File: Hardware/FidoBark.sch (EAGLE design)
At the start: 30 parts, among them T1 BPX81

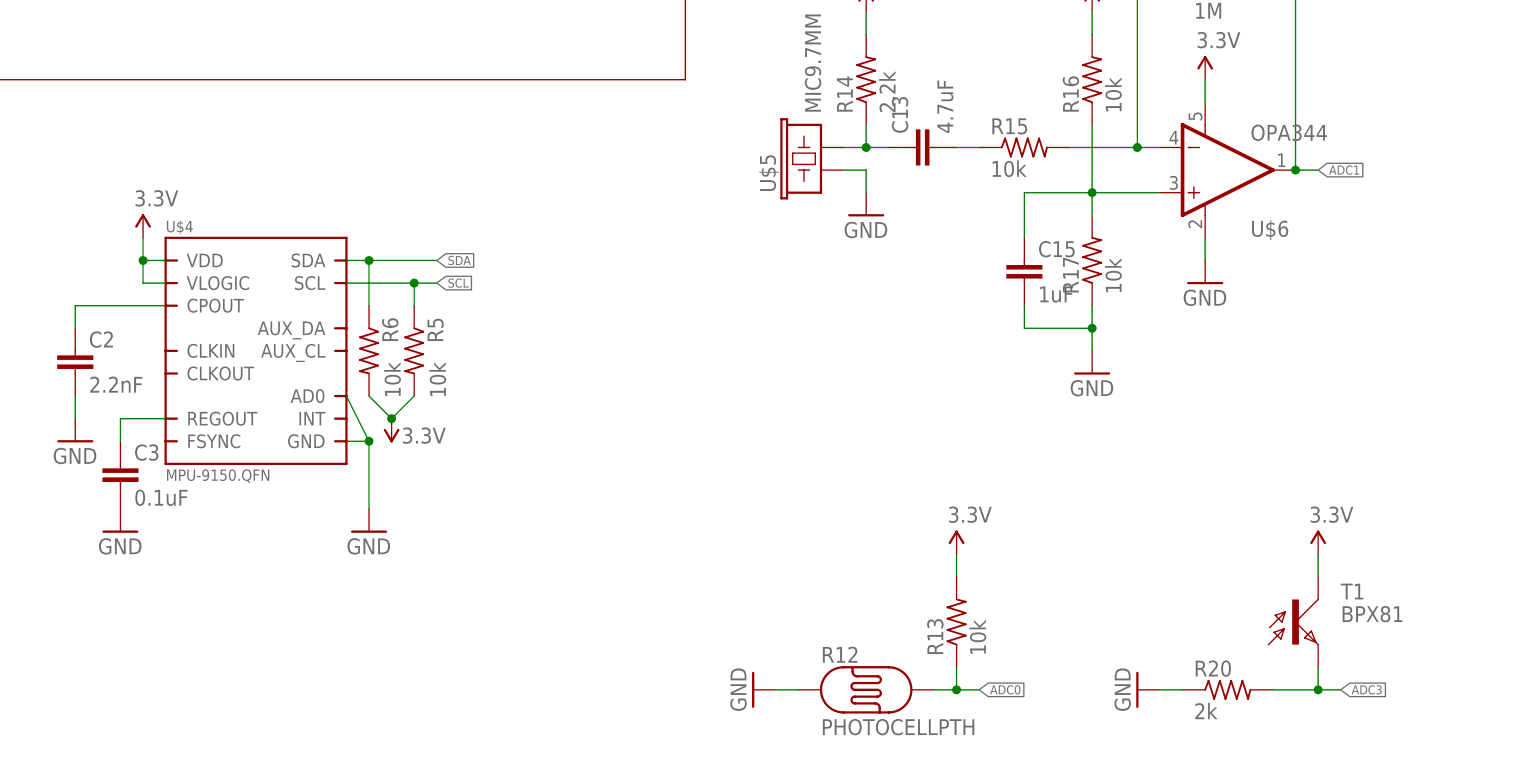
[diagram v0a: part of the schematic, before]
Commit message: battery level sense
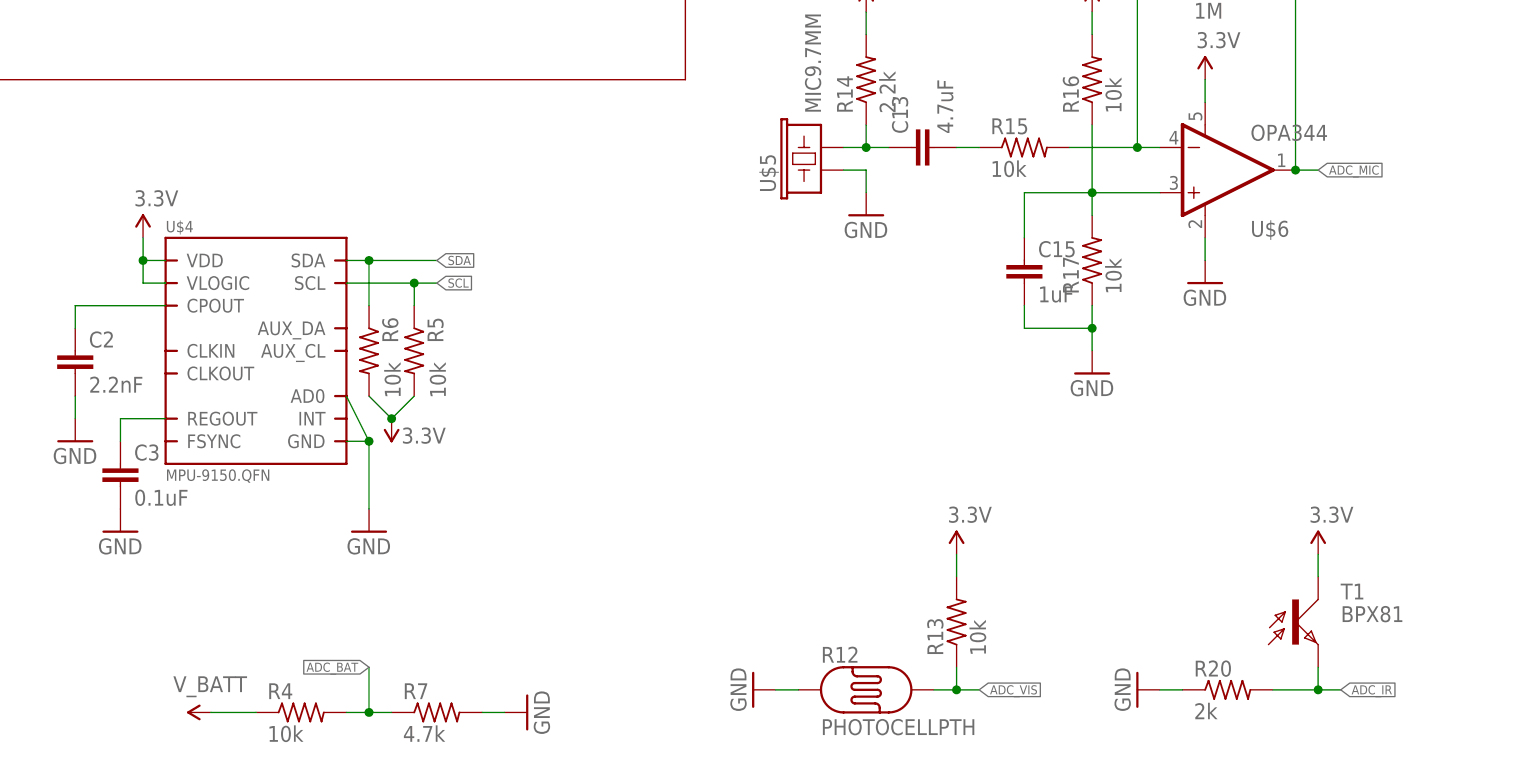
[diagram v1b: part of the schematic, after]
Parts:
- added R4: 10k, rcl:R-US_R0603
- added R7: 4.7k, rcl:R-US_R0603
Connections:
- net ADC0 renamed ADC_VIS
- net ADC1 renamed ADC_MIC
- net ADC3 renamed ADC_IR
- new net ADC_BAT: R4.2, R7.1
- net GND: now also R7.2
- net V_BATT: now also R4.1
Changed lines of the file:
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@@
 <part name="SUPPLY25" library="SparkFun-Aesthetics" deviceset="3.3V" device=""/>
 <part name="R20" library="adafruit" deviceset="R-US_" device="R0603" value="2k"/>
+<part name="R4" library="rcl" deviceset="R-US_" device="R0603" value="10k"/>
+<part name="R7" library="rcl" deviceset="R-US_" device="R0603" value="4.7k"/>
+<part name="SUPPLY7" library="SparkFun-Aesthetics" deviceset="V_BATT" device=""/>
+<part name="GND11" library="SparkFun-Aesthetics" deviceset="GND" device=""/>
 </parts>
 <sheets>
@@
 <instance part="SUPPLY25" gate="G$1" x="162.56" y="68.58"/>
 <instance part="R20" gate="G$1" x="152.4" y="53.34"/>
+<instance part="R4" gate="G$1" x="48.26" y="50.8"/>
+<instance part="R7" gate="G$1" x="63.5" y="50.8"/>
+<instance part="SUPPLY7" gate="G$1" x="38.1" y="50.8" smashed="yes" rot="R90">
+<attribute name="VALUE" x="42.164" y="54.864" size="1.778" layer="96" rot="R180"/>
+</instance>
+<instance part="GND11" gate="1" x="73.66" y="50.8" rot="R90"/>
 </instances>
 <busses>
@@
 <pinref part="R20" gate="G$1" pin="1"/>
 </segment>
+<segment>
+<pinref part="R7" gate="G$1" pin="2"/>
+<pinref part="GND11" gate="1" pin="GND"/>
+<wire x1="68.58" y1="50.8" x2="71.12" y2="50.8" width="0.1524" layer="91"/>
+</segment>
 </net>
 <net name="MOSI" class="0">
@@
 <junction x="63.5" y="205.74"/>
 </segment>
+<segment>
+<pinref part="SUPPLY7" gate="G$1" pin="V_BATT"/>
+<pinref part="R4" gate="G$1" pin="1"/>
+<wire x1="38.1" y1="50.8" x2="43.18" y2="50.8" width="0.1524" layer="91"/>
+</segment>
 </net>
 <net name="N$2" class="0">
@@
 </segment>
 </net>
-<net name="ADC0" class="0">
+<net name="ADC_VIS" class="0">
 <segment>
 <pinref part="R12" gate="G$1" pin="P$2"/>
@@
 </segment>
 </net>
-<net name="ADC1" class="0">
+<net name="ADC_MIC" class="0">
 <segment>
 <pinref part="U$6" gate="G$1" pin="OUT"/>
@@
 </segment>
 </net>
-<net name="ADC3" class="0">
+<net name="ADC_IR" class="0">
 <segment>
 <wire x1="157.48" y1="53.34" x2="162.56" y2="53.34" width="0.1524" layer="91"/>
@@
 </segment>
 </net>
+<net name="ADC_BAT" class="0">
+<segment>
+<pinref part="R4" gate="G$1" pin="2"/>
+<pinref part="R7" gate="G$1" pin="1"/>
+<wire x1="53.34" y1="50.8" x2="55.88" y2="50.8" width="0.1524" layer="91"/>
+<wire x1="55.88" y1="50.8" x2="58.42" y2="50.8" width="0.1524" layer="91"/>
+<wire x1="55.88" y1="50.8" x2="55.88" y2="55.88" width="0.1524" layer="91"/>
+<junction x="55.88" y="50.8"/>
+<label x="55.88" y="55.88" size="1.016" layer="95" rot="R180" xref="yes"/>
+</segment>
+</net>

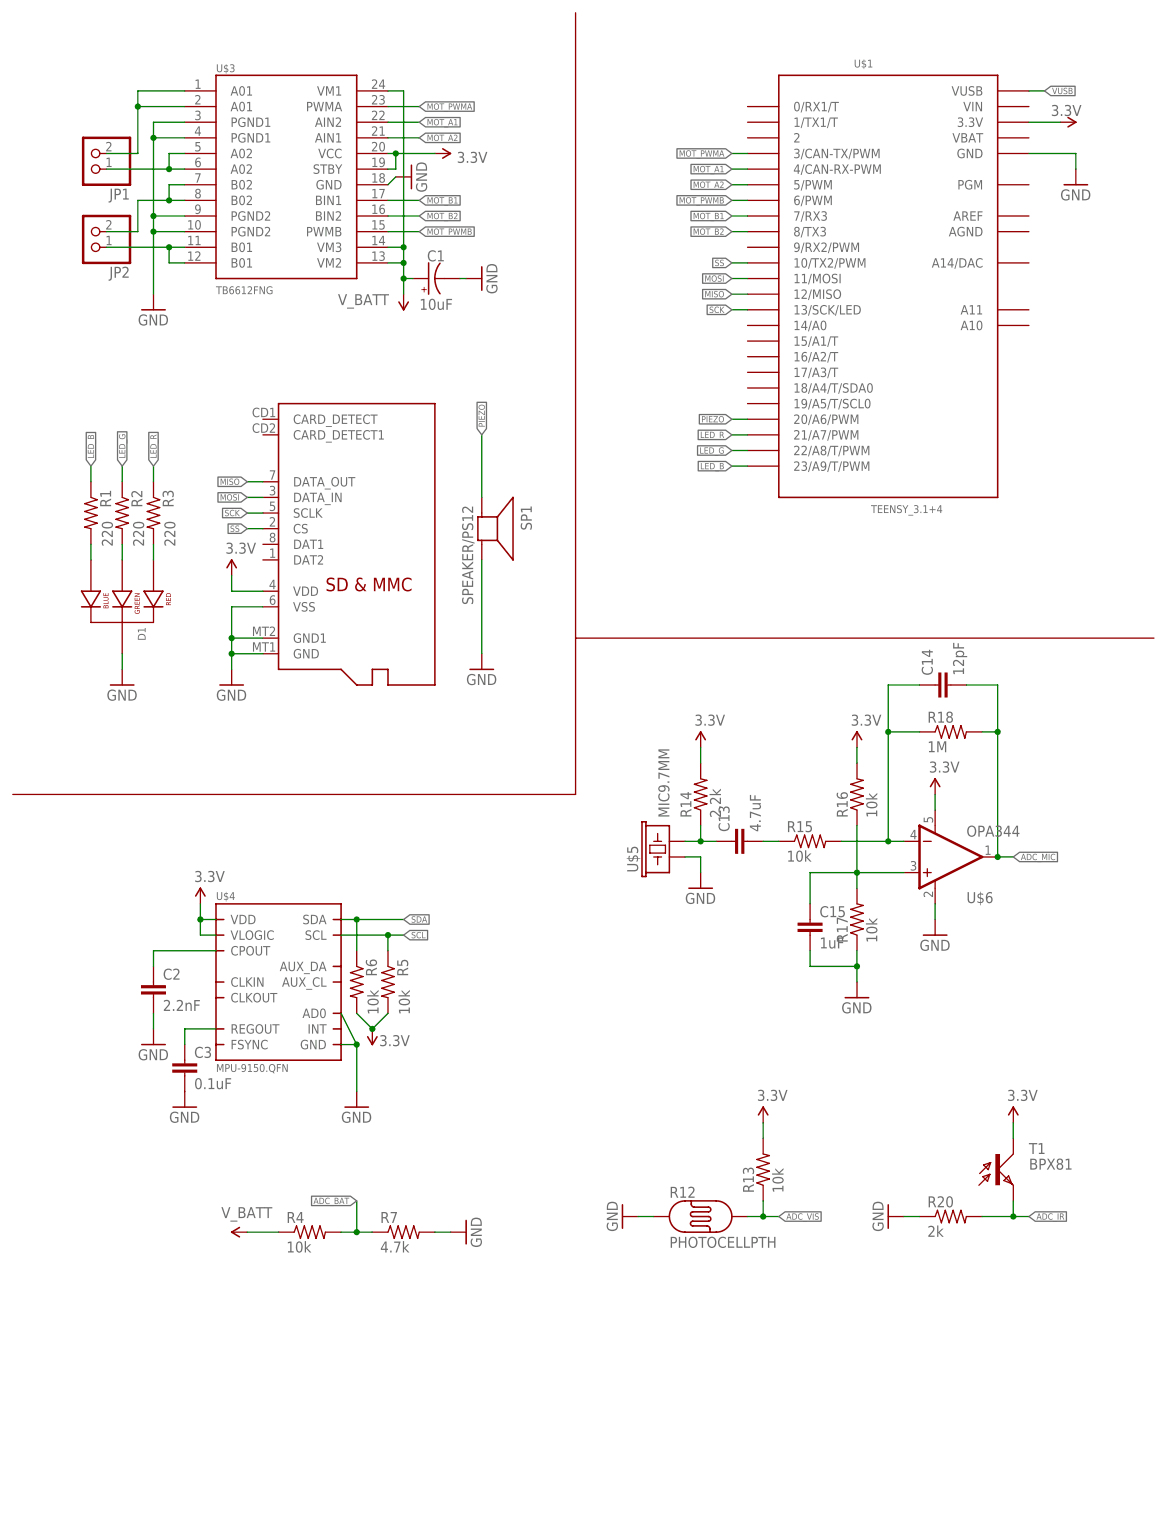
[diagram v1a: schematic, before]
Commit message: added Bluetooth 4.0 Low Energy
should be relatively simple now to interface over an IOS/Android app to
check battery life, download neural nets, etc
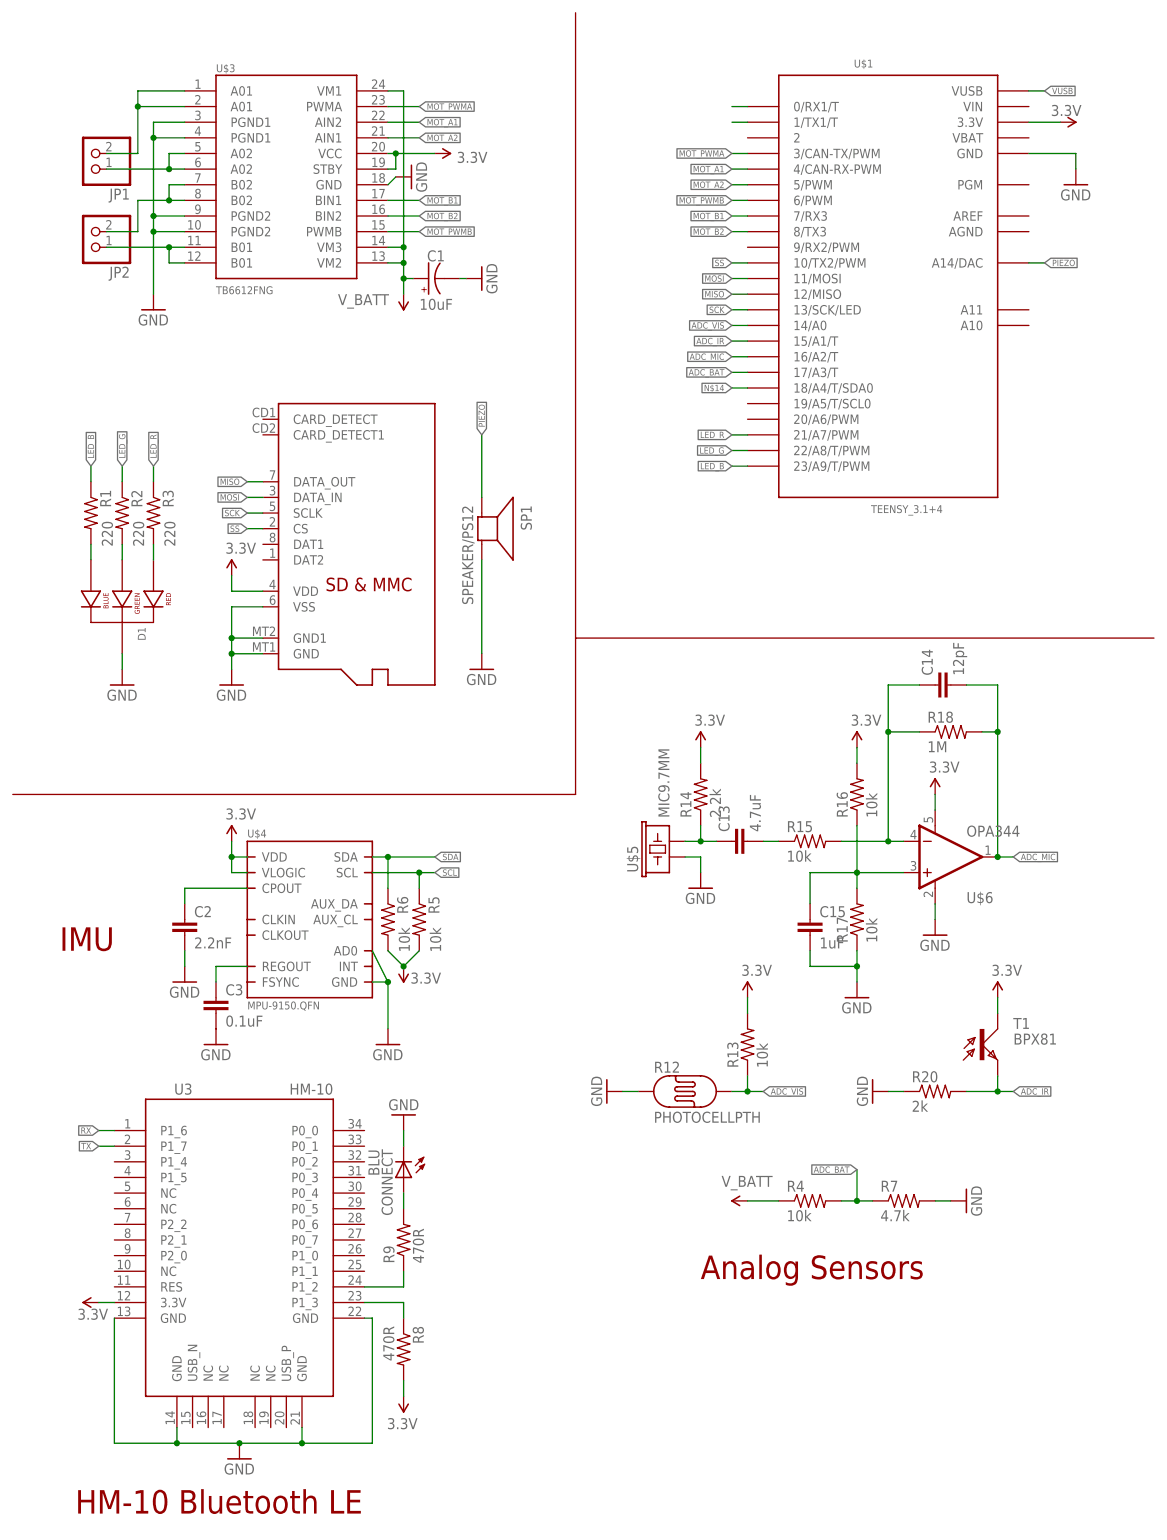
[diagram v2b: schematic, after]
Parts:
- added CONNECT: BLU, adafruit:LEDCHIPLED_0805
- added R8, R9: 470R, SparkFun-Resistors:0.3OHM-1/8W-1%(0805)
- added U3: HM-10, HM-10_BLE:HM-10
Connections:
- new net N$10: R9.1, U3.P1_2
- new net N$11: R8.1, U3.P1_3
- new net N$12: U$1.0/RX1/T
- new net N$13: U$1.1/TX1/T
- new net N$14: U$1.18/A4/T/SDA0
- new net N$16: CONNECT.A, R9.2
- new net RX: U3.P1_6
- new net TX: U3.P1_7
- net 3.3V: now also R8.2, U3.3.3V
- net ADC_BAT: now also U$1.17/A3/T
- net ADC_IR: now also U$1.15/A1/T
- net ADC_MIC: now also U$1.16/A2/T
- net ADC_VIS: now also U$1.14/A0
- net GND: now also CONNECT.C, U3.GND@1, U3.GND@2, U3.GND@3, U3.GND@4
- net PIEZO: now also U$1.A14/DAC; no longer U$1.20/A6/PWM
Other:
- note added: "Analog Sensors"
- note added: "HM-10 Bluetooth LE"
- note added: "IMU"
- moved on the sheet: C2, C3, R12, R13, R20, R4, R5, R6, R7, T1, U$4

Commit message: cosmetics and routing prep
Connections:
- removed net N$12: U$1.0/RX1/T
- removed net N$13: U$1.1/TX1/T
- removed net N$14: U$1.18/A4/T/SDA0
- net RX: now also U$1.0/RX1/T
- net TX: now also U$1.1/TX1/T
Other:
- note added: "1.0"
- note added: "Dual Motor Driver"
- note added: "Fido Prototype PCB"
- note added: "Joshua Gruenstein and Michael Truell"
- note added: "MicroSD Card"
- note added: "RGB LED"
- note added: "Teensy 3.1"
- moved on the sheet: C1, JP1, JP2, U$3

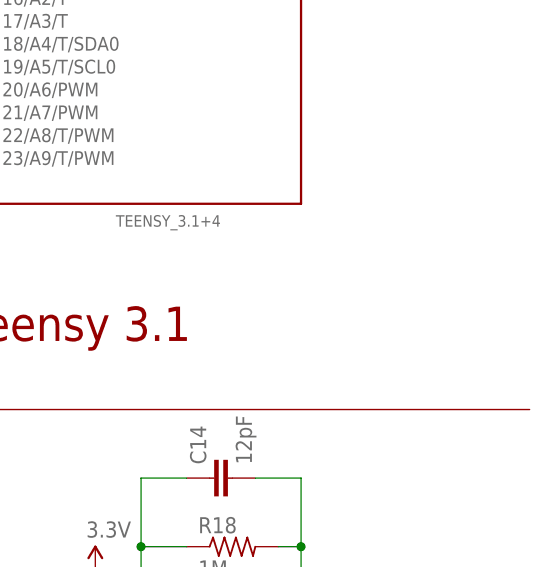
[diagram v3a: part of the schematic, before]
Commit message: added a power jack
oopsy
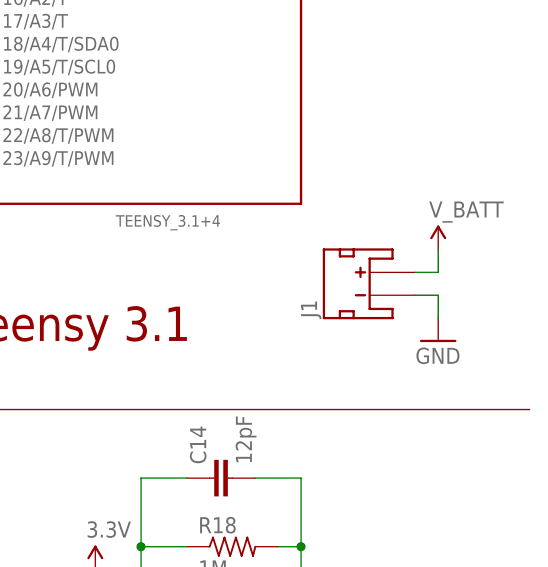
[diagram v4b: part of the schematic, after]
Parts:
- added J1: (no value), SparkFun-Connectors:JST_2MM_MALE
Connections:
- net GND: now also J1.-
- net V_BATT: now also J1.+
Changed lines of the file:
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@@
 <setting verticaltext="up"/>
 </settings>
-<grid distance="0.1" unitdist="inch" unit="inch" style="lines" multiple="1" display="no" altdistance="0.05" altunitdist="inch" altunit="inch"/>
+<grid distance="0.1" unitdist="inch" unit="inch" style="lines" multiple="1" display="no" altdistance="0.01" altunitdist="inch" altunit="inch"/>
 <layers>
 <layer number="1" name="Top" color="4" fill="1" visible="no" active="no"/>
@@
 <part name="SUPPLY8" library="SparkFun-Aesthetics" deviceset="3.3V" device=""/>
 <part name="SUPPLY11" library="SparkFun-Aesthetics" deviceset="3.3V" device=""/>
+<part name="SUPPLY9" library="SparkFun-Aesthetics" deviceset="V_BATT" device=""/>
+<part name="GND12" library="supply1" deviceset="GND" device=""/>
+<part name="J1" library="SparkFun-Connectors" deviceset="JST_2MM_MALE" device=""/>
 </parts>
 <sheets>
@@
 <attribute name="VALUE" x="65.786" y="20.574" size="1.778" layer="96" rot="R180"/>
 </instance>
+<instance part="SUPPLY9" gate="G$1" x="175.26" y="165.1"/>
+<instance part="GND12" gate="1" x="175.26" y="154.94"/>
+<instance part="J1" gate="G$1" x="167.64" y="160.02" rot="R90"/>
 </instances>
 <busses>
@@
 <wire x1="63.5" y1="67.31" x2="63.5" y2="64.77" width="0.1524" layer="91"/>
 </segment>
+<segment>
+<pinref part="GND12" gate="1" pin="GND"/>
+<wire x1="175.26" y1="160.02" x2="175.26" y2="157.48" width="0.1524" layer="91"/>
+<pinref part="J1" gate="G$1" pin="-"/>
+<wire x1="172.72" y1="160.02" x2="175.26" y2="160.02" width="0.1524" layer="91"/>
+</segment>
 </net>
 <net name="MOSI" class="0">
@@
 <wire x1="119.38" y1="55.88" x2="124.46" y2="55.88" width="0.1524" layer="91"/>
 </segment>
-</net>
+<segment>
+<pinref part="SUPPLY9" gate="G$1" pin="V_BATT"/>
+<wire x1="175.26" y1="162.56" x2="175.26" y2="165.1" width="0.1524" layer="91"/>
+<pinref part="J1" gate="G$1" pin="+"/>
+<wire x1="175.26" y1="162.56" x2="172.72" y2="162.56" width="0.1524" layer="91"/>
+</segment>
+</net>
